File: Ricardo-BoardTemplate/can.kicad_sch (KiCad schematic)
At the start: 11 parts, among them U4 SN65HVD230

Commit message: most FP assignments to 0402
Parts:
- C33, C35, C36, C37: footprint Capacitor_SMD:C_0603_1608Metric -> Capacitor_SMD:C_0402_1005Metric
- R28, R29, R30: footprint Resistor_SMD:R_0603_1608Metric -> Resistor_SMD:R_0402_1005Metric
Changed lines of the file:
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@@
       (effects (font (size 1.27 1.27)) (justify right))
     )
-    (property "Footprint" "Capacitor_SMD:C_0603_1608Metric" (id 2) (at 175.26 82.55 0)
+    (property "Footprint" "Capacitor_SMD:C_0402_1005Metric" (id 2) (at 175.26 82.55 0)
       (effects (font (size 1.27 1.27)) hide)
     )
@@
       (effects (font (size 1.27 1.27)) (justify left))
     )
-    (property "Footprint" "Capacitor_SMD:C_0603_1608Metric" (id 2) (at 121.92 71.12 0)
+    (property "Footprint" "Capacitor_SMD:C_0402_1005Metric" (id 2) (at 121.92 71.12 0)
       (effects (font (size 1.27 1.27)) hide)
     )
@@
       (effects (font (size 1.27 1.27)) (justify left))
     )
-    (property "Footprint" "Resistor_SMD:R_0603_1608Metric" (id 2) (at 124.46 95.25 0)
+    (property "Footprint" "Resistor_SMD:R_0402_1005Metric" (id 2) (at 124.46 95.25 0)
       (effects (font (size 1.27 1.27)) hide)
     )
@@
       (effects (font (size 1.27 1.27)) (justify left))
     )
-    (property "Footprint" "Resistor_SMD:R_0603_1608Metric" (id 2) (at 165.862 93.98 90)
+    (property "Footprint" "Resistor_SMD:R_0402_1005Metric" (id 2) (at 165.862 93.98 90)
       (effects (font (size 1.27 1.27)) hide)
     )
@@
       (effects (font (size 1.27 1.27)) (justify left))
     )
-    (property "Footprint" "Resistor_SMD:R_0603_1608Metric" (id 2) (at 165.862 83.82 90)
+    (property "Footprint" "Resistor_SMD:R_0402_1005Metric" (id 2) (at 165.862 83.82 90)
       (effects (font (size 1.27 1.27)) hide)
     )
@@
     (property "Reference" "C35" (id 0) (at 171.45 82.55 90))
     (property "Value" "0.1uF" (id 1) (at 171.45 85.09 90))
-    (property "Footprint" "Capacitor_SMD:C_0603_1608Metric" (id 2) (at 175.26 87.9348 0)
+    (property "Footprint" "Capacitor_SMD:C_0402_1005Metric" (id 2) (at 175.26 87.9348 0)
       (effects (font (size 1.27 1.27)) hide)
     )
@@
       (effects (font (size 1.27 1.27)) (justify right))
     )
-    (property "Footprint" "Capacitor_SMD:C_0603_1608Metric" (id 2) (at 175.26 100.33 0)
+    (property "Footprint" "Capacitor_SMD:C_0402_1005Metric" (id 2) (at 175.26 100.33 0)
       (effects (font (size 1.27 1.27)) hide)
     )

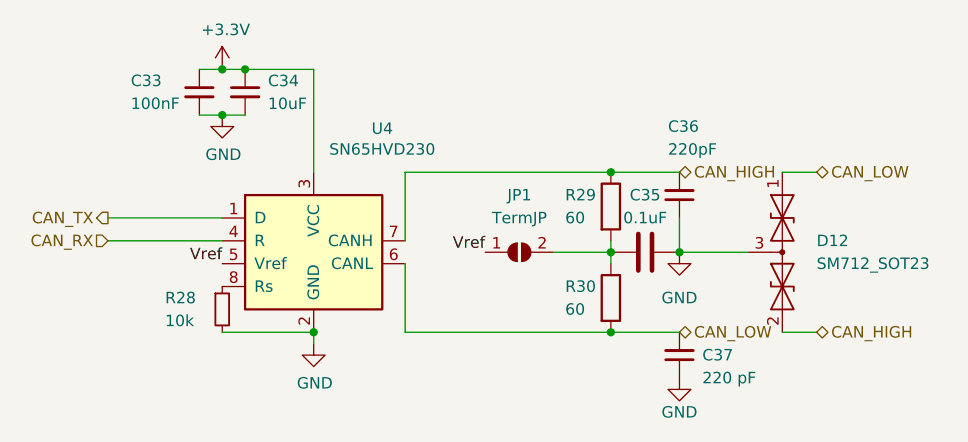
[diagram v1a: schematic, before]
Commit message: Finished power schematic, layout template still left to do.
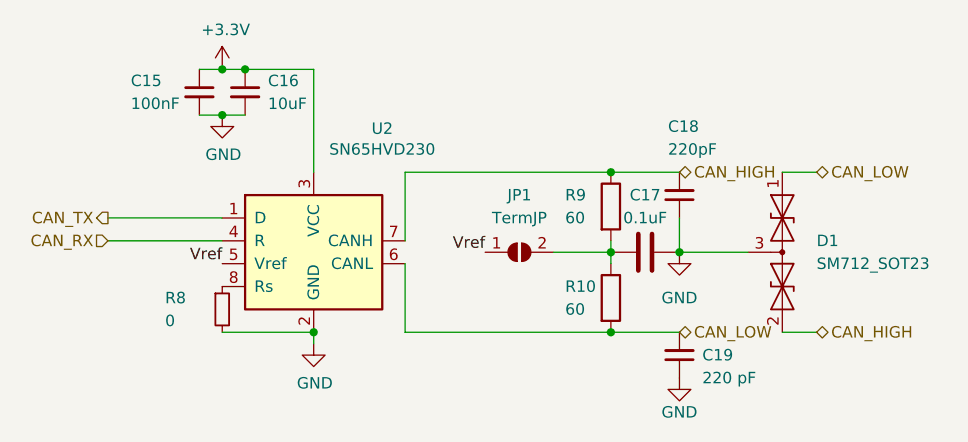
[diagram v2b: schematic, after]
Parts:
- C16: renamed from C34; footprint Capacitor_SMD:C_0603_1608Metric -> Capacitor_SMD:C_0402_1005Metric
- JP1: footprint (none) -> Jumper:SolderJumper-2_P1.3mm_Open_RoundedPad1.0x1.5mm
- R8: renamed from R28; value 10k -> 0; footprint Resistor_SMD:R_0402_1005Metric -> Resistor_SMD:R_0603_1608Metric
- renumbered C33 to C15, C35 to C17, C36 to C18, C37 to C19, D12 to D1, R30 to R10, R29 to R9, U4 to U2
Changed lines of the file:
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@@
   (symbol (lib_id "power:GND") (at 134.62 99.06 0) (unit 1)
     (in_bom yes) (on_board yes) (fields_autoplaced)
-    (property "Reference" "#PWR0130" (id 0) (at 134.62 105.41 0)
+    (property "Reference" "#PWR026" (id 0) (at 134.62 105.41 0)
       (effects (font (size 1.27 1.27)) hide)
     )
@@
   (symbol (lib_id "power:+3.3V") (at 124.46 68.58 0) (unit 1)
     (in_bom yes) (on_board yes) (fields_autoplaced)
-    (property "Reference" "#PWR0131" (id 0) (at 124.46 72.39 0)
+    (property "Reference" "#PWR024" (id 0) (at 124.46 72.39 0)
       (effects (font (size 1.27 1.27)) hide)
     )
@@
   (symbol (lib_id "Interface_CAN_LIN:SN65HVD230") (at 134.62 87.63 0) (unit 1)
     (in_bom yes) (on_board yes) (fields_autoplaced)
-    (property "Reference" "U4" (id 0) (at 142.24 75.1586 0))
+    (property "Reference" "U2" (id 0) (at 142.24 75.1586 0))
     (property "Value" "SN65HVD230" (id 1) (at 142.24 77.47 0))
     (property "Footprint" "Package_SO:SOIC-8_3.9x4.9mm_P1.27mm" (id 2) (at 134.62 100.33 0)
@@
   (symbol (lib_id "Device:C_Small") (at 127 71.12 0) (unit 1)
     (in_bom yes) (on_board yes) (fields_autoplaced)
-    (property "Reference" "C34" (id 0) (at 129.54 69.8562 0)
+    (property "Reference" "C16" (id 0) (at 129.54 69.8562 0)
       (effects (font (size 1.27 1.27)) (justify left))
     )
@@
       (effects (font (size 1.27 1.27)) (justify left))
     )
-    (property "Footprint" "Capacitor_SMD:C_0603_1608Metric" (id 2) (at 127 71.12 0)
+    (property "Footprint" "Capacitor_SMD:C_0402_1005Metric" (id 2) (at 127 71.12 0)
       (effects (font (size 1.27 1.27)) hide)
     )
@@
   (symbol (lib_id "Device:C_Small") (at 175.26 82.55 180) (unit 1)
     (in_bom yes) (on_board yes)
-    (property "Reference" "C36" (id 0) (at 173.99 74.93 0)
+    (property "Reference" "C18" (id 0) (at 173.99 74.93 0)
       (effects (font (size 1.27 1.27)) (justify right))
     )
@@
   (symbol (lib_id "Diode:SM712_SOT23") (at 186.69 88.9 270) (unit 1)
     (in_bom yes) (on_board yes) (fields_autoplaced)
-    (property "Reference" "D12" (id 0) (at 190.5 87.63 90)
+    (property "Reference" "D1" (id 0) (at 190.5 87.63 90)
       (effects (font (size 1.27 1.27)) (justify left))
     )
@@
   (symbol (lib_id "power:GND") (at 175.26 88.9 0) (unit 1)
     (in_bom yes) (on_board yes) (fields_autoplaced)
-    (property "Reference" "#PWR0146" (id 0) (at 175.26 95.25 0)
+    (property "Reference" "#PWR027" (id 0) (at 175.26 95.25 0)
       (effects (font (size 1.27 1.27)) hide)
     )
@@
   (symbol (lib_id "power:GND") (at 175.26 102.87 0) (unit 1)
     (in_bom yes) (on_board yes) (fields_autoplaced)
-    (property "Reference" "#PWR0151" (id 0) (at 175.26 109.22 0)
+    (property "Reference" "#PWR028" (id 0) (at 175.26 109.22 0)
       (effects (font (size 1.27 1.27)) hide)
     )
@@
   (symbol (lib_id "Device:C_Small") (at 121.92 71.12 0) (unit 1)
     (in_bom yes) (on_board yes) (fields_autoplaced)
-    (property "Reference" "C33" (id 0) (at 114.3 69.85 0)
+    (property "Reference" "C15" (id 0) (at 114.3 69.85 0)
       (effects (font (size 1.27 1.27)) (justify left))
     )
@@
   (symbol (lib_id "Device:R_Small") (at 124.46 95.25 0) (unit 1)
     (in_bom yes) (on_board yes)
-    (property "Reference" "R28" (id 0) (at 118.11 93.98 0)
-      (effects (font (size 1.27 1.27)) (justify left))
-    )
-    (property "Value" "10k" (id 1) (at 118.11 96.52 0)
-      (effects (font (size 1.27 1.27)) (justify left))
-    )
-    (property "Footprint" "Resistor_SMD:R_0402_1005Metric" (id 2) (at 124.46 95.25 0)
+    (property "Reference" "R8" (id 0) (at 118.11 93.98 0)
+      (effects (font (size 1.27 1.27)) (justify left))
+    )
+    (property "Value" "0" (id 1) (at 118.11 96.52 0)
+      (effects (font (size 1.27 1.27)) (justify left))
+    )
+    (property "Footprint" "Resistor_SMD:R_0603_1608Metric" (id 2) (at 124.46 95.25 0)
       (effects (font (size 1.27 1.27)) hide)
     )
@@
   (symbol (lib_id "Device:R") (at 167.64 93.98 0) (unit 1)
     (in_bom yes) (on_board yes) (fields_autoplaced)
-    (property "Reference" "R30" (id 0) (at 162.56 92.71 0)
+    (property "Reference" "R10" (id 0) (at 162.56 92.71 0)
       (effects (font (size 1.27 1.27)) (justify left))
     )
@@
   (symbol (lib_id "Device:R") (at 167.64 83.82 0) (unit 1)
     (in_bom yes) (on_board yes) (fields_autoplaced)
-    (property "Reference" "R29" (id 0) (at 162.56 82.55 0)
+    (property "Reference" "R9" (id 0) (at 162.56 82.55 0)
       (effects (font (size 1.27 1.27)) (justify left))
     )
@@
   (symbol (lib_id "Device:C") (at 171.45 88.9 90) (unit 1)
     (in_bom yes) (on_board yes) (fields_autoplaced)
-    (property "Reference" "C35" (id 0) (at 171.45 82.55 90))
+    (property "Reference" "C17" (id 0) (at 171.45 82.55 90))
     (property "Value" "0.1uF" (id 1) (at 171.45 85.09 90))
     (property "Footprint" "Capacitor_SMD:C_0402_1005Metric" (id 2) (at 175.26 87.9348 0)
@@
   (symbol (lib_id "power:GND") (at 124.46 73.66 0) (unit 1)
     (in_bom yes) (on_board yes) (fields_autoplaced)
-    (property "Reference" "#PWR0145" (id 0) (at 124.46 80.01 0)
+    (property "Reference" "#PWR025" (id 0) (at 124.46 80.01 0)
       (effects (font (size 1.27 1.27)) hide)
     )
@@
     (property "Reference" "JP1" (id 0) (at 157.48 82.55 0))
     (property "Value" "TermJP" (id 1) (at 157.48 85.09 0))
-    (property "Footprint" "" (id 2) (at 157.48 88.9 0)
+    (property "Footprint" "Jumper:SolderJumper-2_P1.3mm_Open_RoundedPad1.0x1.5mm" (id 2) (at 157.48 88.9 0)
       (effects (font (size 1.27 1.27)) hide)
     )
@@
   (symbol (lib_id "Device:C_Small") (at 175.26 100.33 180) (unit 1)
     (in_bom yes) (on_board yes) (fields_autoplaced)
-    (property "Reference" "C37" (id 0) (at 177.8 100.33 0)
+    (property "Reference" "C19" (id 0) (at 177.8 100.33 0)
       (effects (font (size 1.27 1.27)) (justify right))
     )

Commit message: Initial buck boost layout
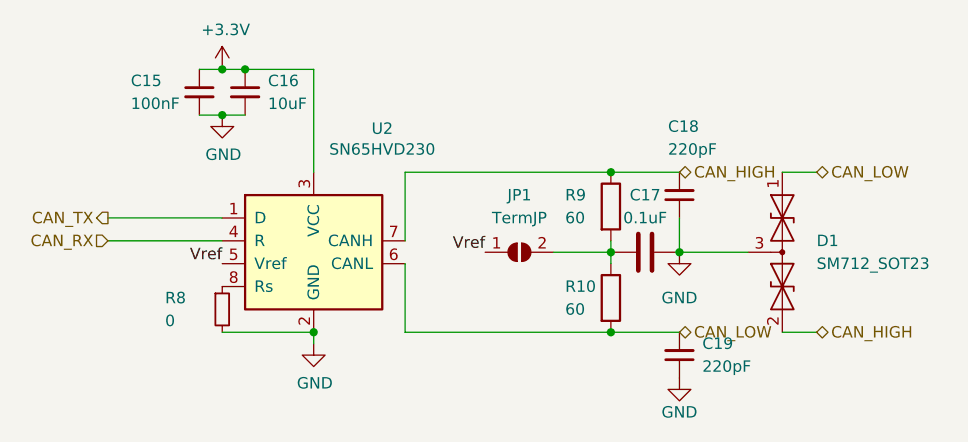
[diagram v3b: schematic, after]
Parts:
- C19: value 220 pF -> 220pF
- JP1: footprint Jumper:SolderJumper-2_P1.3mm_Open_RoundedPad1.0x1.5mm -> (none)
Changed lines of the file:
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@@
     (property "Reference" "JP1" (id 0) (at 157.48 82.55 0))
     (property "Value" "TermJP" (id 1) (at 157.48 85.09 0))
-    (property "Footprint" "Jumper:SolderJumper-2_P1.3mm_Open_RoundedPad1.0x1.5mm" (id 2) (at 157.48 88.9 0)
+    (property "Footprint" "" (id 2) (at 157.48 88.9 0)
       (effects (font (size 1.27 1.27)) hide)
     )
@@
   (symbol (lib_id "Device:C_Small") (at 175.26 100.33 180) (unit 1)
     (in_bom yes) (on_board yes) (fields_autoplaced)
-    (property "Reference" "C19" (id 0) (at 177.8 100.33 0)
+    (property "Reference" "C19" (id 0) (at 177.8 99.0535 0)
       (effects (font (size 1.27 1.27)) (justify right))
     )
-    (property "Value" "220 pF" (id 1) (at 177.8 102.87 0)
+    (property "Value" "220pF" (id 1) (at 177.8 101.5935 0)
       (effects (font (size 1.27 1.27)) (justify right))
     )
